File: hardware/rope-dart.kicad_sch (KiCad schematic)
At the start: 3 parts, among them IC1 MAX4906ELB+T, U1 ESP32-C3-MINI-1, U2 MAX77751FEFG+

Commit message: started charging shematics
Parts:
- removed IC1: MAX4906ELB+T, MAX4906ELBT, symbol MAX4906ELB+T:MAX4906ELB+T
- added BT1: Battery_Cell, symbol Device:Battery_Cell
- added C1, C2, C3, C4: C, symbol Device:C
- added D1, D2: LED, symbol Device:LED
- added IC2: MAX4906ELB+T, MAX4906ELBT, symbol MAX4906ELB+T:MAX4906ELB+T
- added J1: USB_C_Receptacle_USB2.0, symbol Connector:USB_C_Receptacle_USB2.0
- added L1: L, symbol Device:L
- added R1: 24.3k, symbol Device:R
- added R2: 24.9k, symbol Device:R
- added R5, R6: R, symbol Device:R
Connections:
- net GND: now reaches U1.1 (GND), U1.2 (GND), U1.36 (GND), U1.37 (GND), U1.38 (GND), U1.39 (GND), U1.40 (GND), U1.41 (GND), U1.42 (GND), U1.43 (GND), U1.44 (GND), U1.45 (GND), U1.46 (GND), U1.47 (GND), U1.48 (GND), U1.49 (GND), U1.50 (GND), U1.51 (GND), U1.52 (GND), U1.53 (GND)
- net GND: now also U2.10 (VDD), U2.18_19 (PGND), U2.9 (GND), BT1.2 (-), C1.2, C3.2, C4.2, IC2.3 (GND), J1.A1 (GND), J1.A12 (GND), J1.B1 (GND), J1.B12 (GND), R1.2, R2.2
- net at U1.26 (GPIO18/USB_D-): now also IC2.6 (NO2)
- net at U1.27 (GPIO19/USB_D+): now also IC2.7 (NO1)
- net 3V3: now reaches U1.3 (3V3)
- net 3V3: now also IC2.10 (V+)
- net ITOPOFF: now reaches U1.5 (GPIO2/ADC1_CH2)
- net ITOPOFF: now also U2.11 (ITOPOFF), R1.1
- net USB_SWITCH: now reaches U1.6 (GPIO3/ADC1_CH3)
- net USB_SWITCH: now also IC2.1 (IN)
- net at U2.1 (BST): now also C2.1
- net at U2.12 (IFAST): now also R2.1
- net at U2.13_14 (BATT): now also BT1.1 (+)
- net SYS: now reaches U2.15_16 (SYS)
- net SYS: now also C3.1, D1.2 (A), D2.2 (A), L1.2
- net at U2.17 (PVL): now also C1.1
- net INOKB: now reaches U2.2 (INOKB)
- net INOKB: now also R6.2
- net at U2.20_21 (LX): now also C2.2, L1.1
- net at U2.22 (BYP): now also C4.1
- net VBUS: now reaches U2.23_24 (CHGIN)
- net VBUS: now also J1.A4 (VBUS), J1.A9 (VBUS), J1.B4 (VBUS), J1.B9 (VBUS)
- net STAT: now reaches U2.3 (STAT)
- net STAT: now also R5.2
- net CC2: now reaches U2.4 (CC2)
- net CC2: now also J1.B5 (CC2)
- net CC1: now reaches U2.5 (CC1)
- net CC1: now also J1.A5 (CC1)
- net at U2.6 (DP): now also IC2.9 (NC1)
- net at U2.7 (DN): now also IC2.8 (NC2)
- net ENBST: now reaches U2.8 (ENBST)
- new net: D1.1 (K), R5.1
- new net: D2.1 (K), R6.1
- new net D+: IC2.4 (COM1), J1.A6 (D+), J1.B6 (D+)
- new net D-: IC2.5 (COM2), J1.A7 (D-), J1.B7 (D-)
- no-connect marks 0 -> 2
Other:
- moved on the sheet: U1, U2

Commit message: computer swap
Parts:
- removed BT1: Battery_Cell, symbol Device:Battery_Cell
- added BT2: Battery_Cell, symbol Device:Battery_Cell
- added J2: ITOPOFF, symbol Connector:Conn_01x02_Pin
- added J3: USBSWITCH, symbol Connector:Conn_01x02_Pin
- added J4: BATT, symbol Connector:Conn_01x02_Pin
- added J5: Conn_01x02_Socket, symbol Connector:Conn_01x02_Socket
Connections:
- net GND: now also J4.1 (Pin_1)
- net ITOPOFF: now also J2.2 (Pin_2); no longer R1.1, U2.11 (ITOPOFF)
- net USB_SWITCH: now also J3.2 (Pin_2); no longer U1.6 (GPIO3/ADC1_CH3)
- net at U2.13_14 (BATT): now also J4.2 (Pin_2)
- new net: J2.1 (Pin_1), R1.1, U2.11 (ITOPOFF)
- new net: J3.1 (Pin_1), U1.6 (GPIO3/ADC1_CH3)
- new net: BT2.2 (-), J5.1 (Pin_1)
- new net: BT2.1 (+), J5.2 (Pin_2)

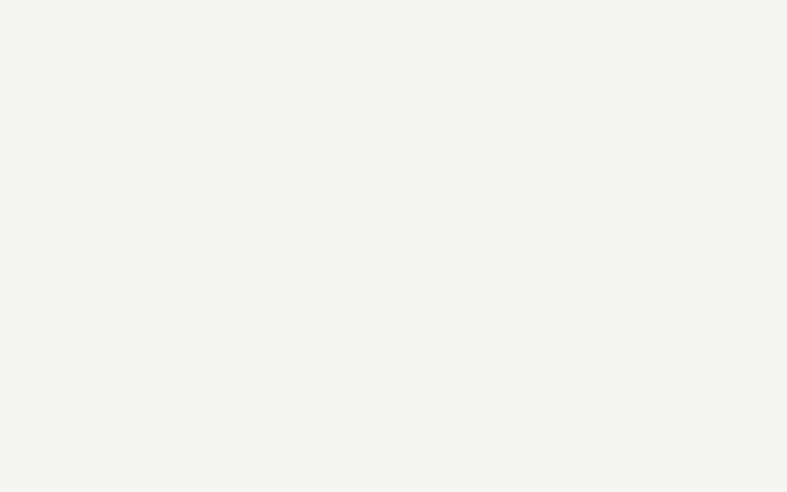
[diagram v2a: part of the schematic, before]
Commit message: splitted schematics into multiple sheets
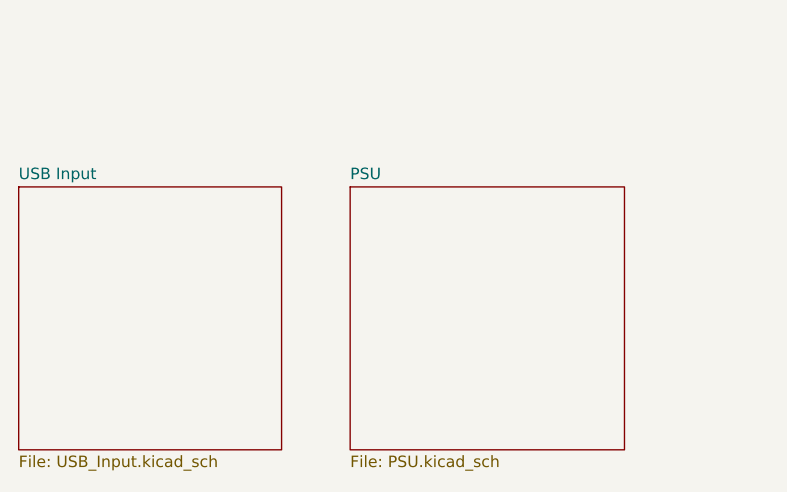
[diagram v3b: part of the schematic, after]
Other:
- added sheet PSU (PSU.kicad_sch)
- added sheet USB Input (USB_Input.kicad_sch)
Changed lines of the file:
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@@
+    )
+  )
+  (sheet (at 29.21 168.91) (size 29.21 29.21) (fields_autoplaced)
+    (stroke (width 0.1524) (type solid))
+    (fill (color 0 0 0 0.0000))
+    (property "Sheetname" "USB Input" (at 29.21 168.1984 0)
+      (effects (font (size 1.27 1.27)) (justify left bottom))
+    )
+    (property "Sheetfile" "USB_Input.kicad_sch" (at 29.21 198.7046 0)
+      (effects (font (size 1.27 1.27)) (justify left top))
+    )
+    (property "Field2" "" (at 29.21 168.91 0)
+      (effects (font (size 1.27 1.27)) hide)
+    )
+    (instances
+      (project "rope-dart"
+        (path "/862cf1c6-cdba-429f-8e57-9bd700b495f1" (page "3"))
+      )
+    )
+  )
+  (sheet (at 66.04 168.91) (size 30.48 29.21) (fields_autoplaced)
+    (stroke (width 0.1524) (type solid))
+    (fill (color 0 0 0 0.0000))
+    (property "Sheetname" "PSU" (at 66.04 168.1984 0)
+      (effects (font (size 1.27 1.27)) (justify left bottom))
+    )
+    (property "Sheetfile" "PSU.kicad_sch" (at 66.04 198.7046 0)
+      (effects (font (size 1.27 1.27)) (justify left top))
+    )
+    (instances
+      (project "rope-dart"
+        (path "/862cf1c6-cdba-429f-8e57-9bd700b495f1" (page "2"))
+      )
     )
   )

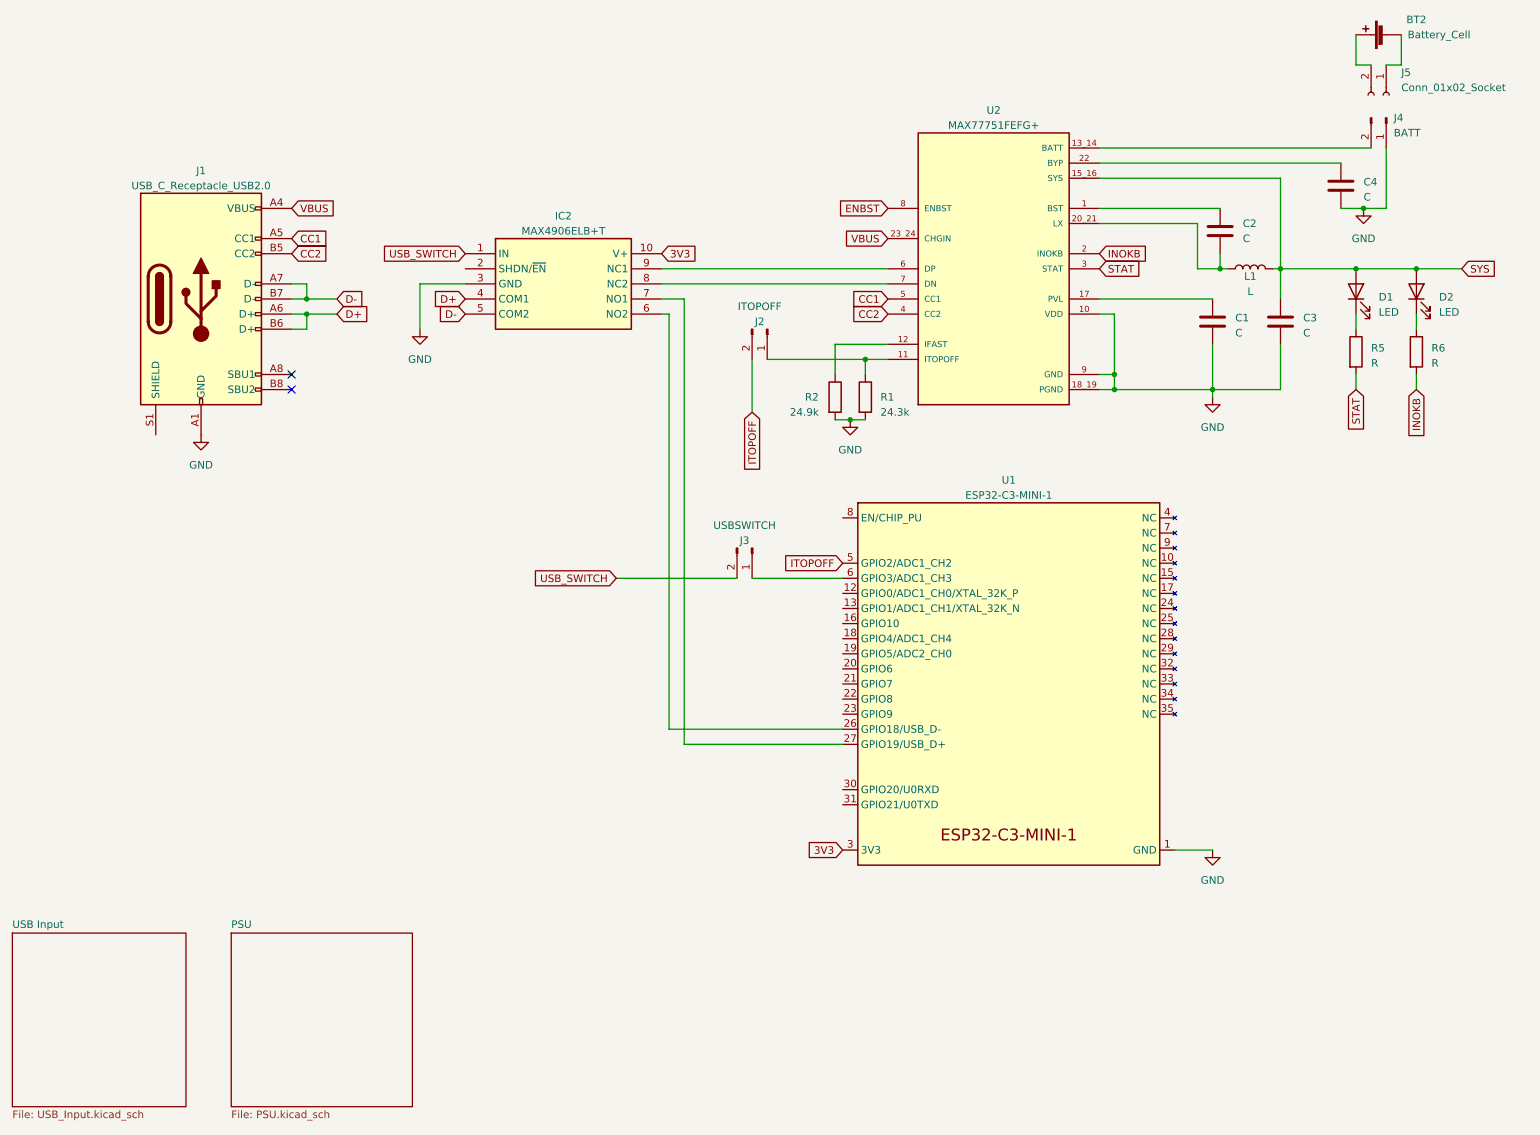
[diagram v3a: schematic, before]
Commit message: added cpu sheet and removed unused circuits
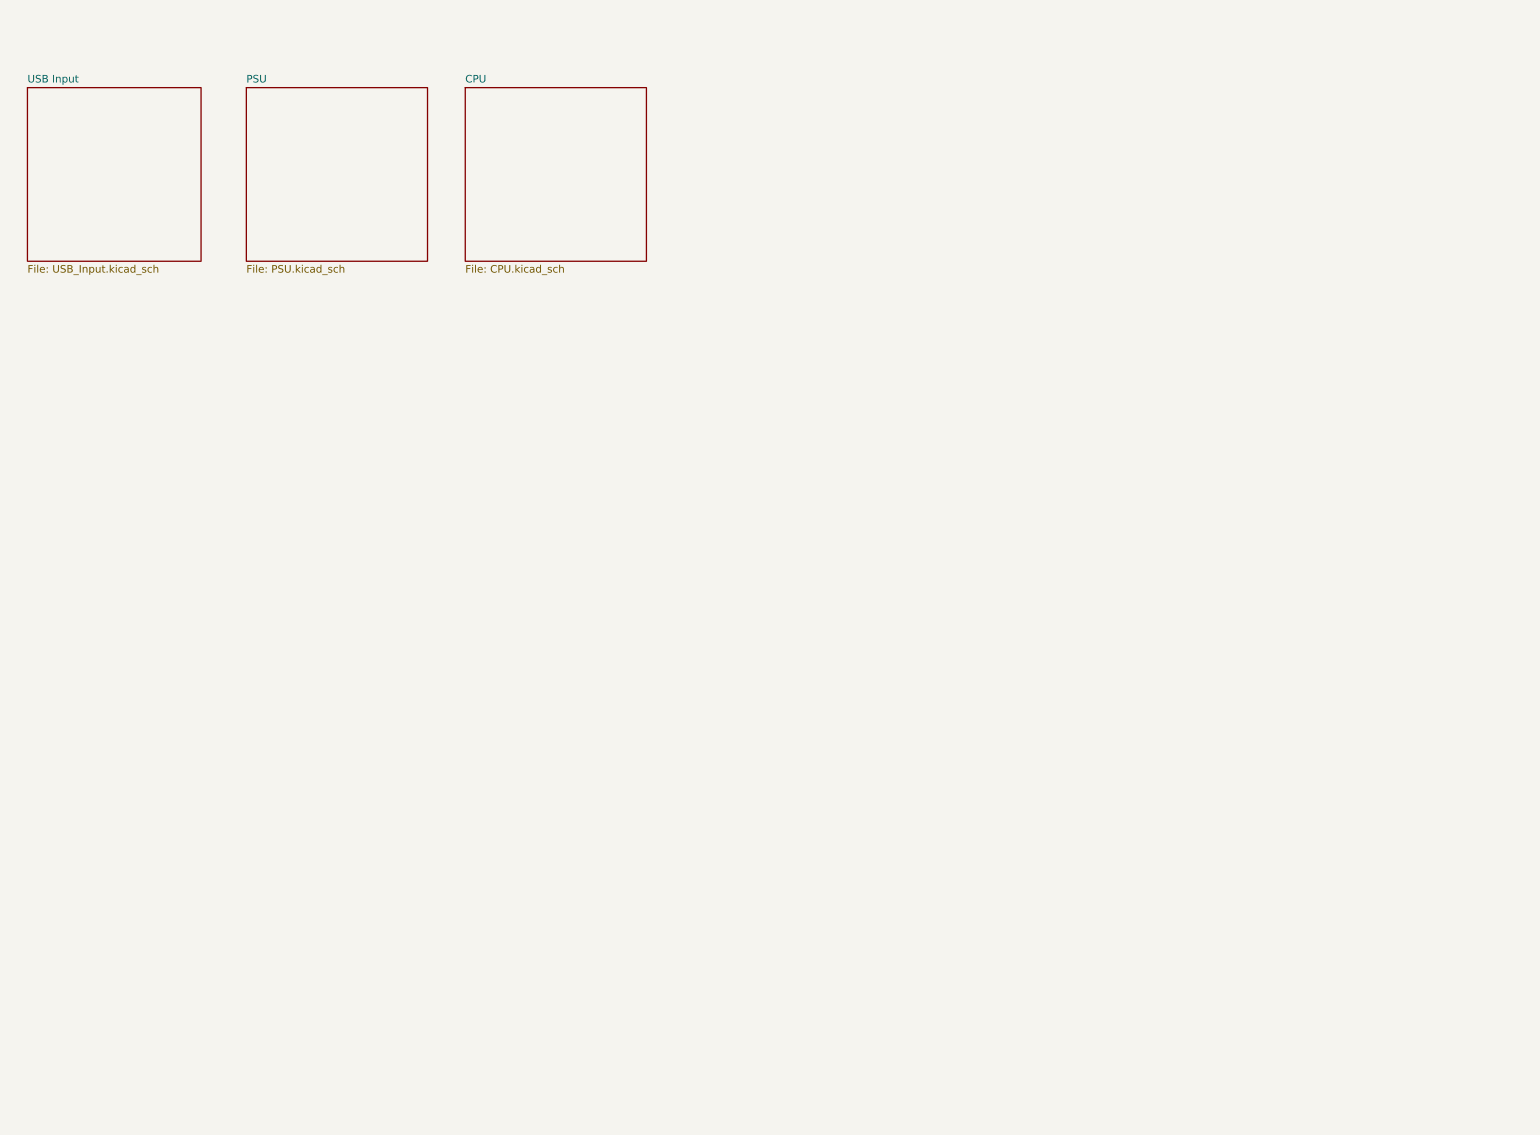
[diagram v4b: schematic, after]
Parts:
- removed BT2: Battery_Cell, symbol Device:Battery_Cell
- removed C1, C2, C3, C4: C, symbol Device:C
- removed D1, D2: LED, symbol Device:LED
- removed IC2: MAX4906ELB+T, MAX4906ELBT, symbol MAX4906ELB+T:MAX4906ELB+T
- removed J1: USB_C_Receptacle_USB2.0, symbol Connector:USB_C_Receptacle_USB2.0
- removed J2: ITOPOFF, symbol Connector:Conn_01x02_Pin
- removed J3: USBSWITCH, symbol Connector:Conn_01x02_Pin
- removed J4: BATT, symbol Connector:Conn_01x02_Pin
- removed J5: Conn_01x02_Socket, symbol Connector:Conn_01x02_Socket
- removed L1: L, symbol Device:L
- removed R1: 24.3k, symbol Device:R
- removed R2: 24.9k, symbol Device:R
- removed R5, R6: R, symbol Device:R
- removed U1: ESP32-C3-MINI-1, Espressif:ESP32-C3-MINI-1, symbol Espressif:ESP32-C3-MINI-1
- removed U2: MAX77751FEFG+, IC_MAX77751FEFG+, symbol MAX77751FEFG_:MAX77751FEFG+
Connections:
- no-connect marks 2 -> 0
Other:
- added sheet CPU (CPU.kicad_sch)
